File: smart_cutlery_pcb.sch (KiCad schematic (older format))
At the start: 0 parts

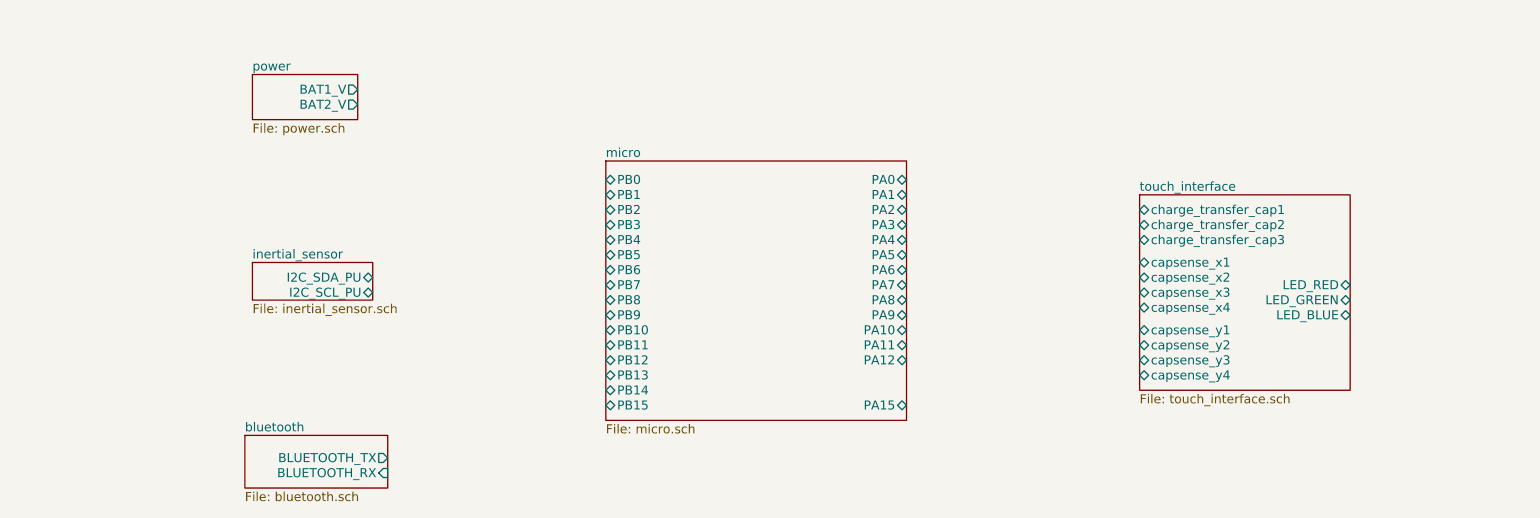
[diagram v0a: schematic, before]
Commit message: Make top-level connections between microcontroller and everything else
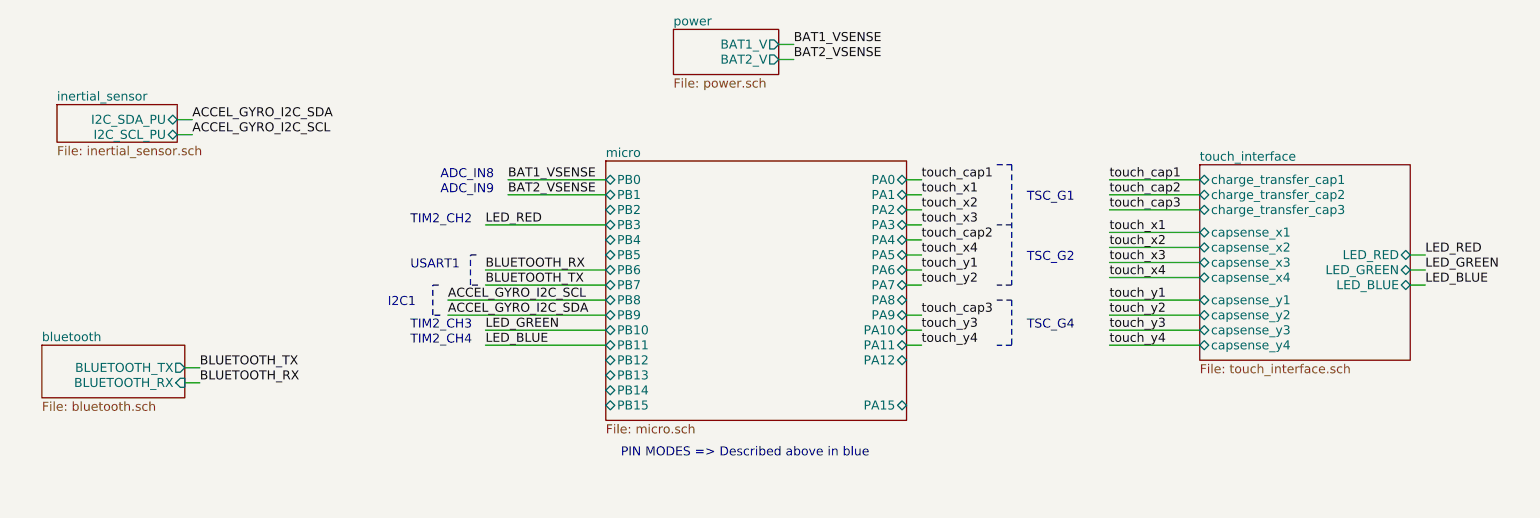
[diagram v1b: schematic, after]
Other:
- note added: "ADC_IN8"
- note added: "ADC_IN9"
- note added: "I2C1"
- note added: "PIN MODES => Described above in blue"
- note added: "TIM2_CH2"
- note added: "TIM2_CH3"
- note added: "TIM2_CH4\n"
- note added: "TSC_G1"
- note added: "TSC_G2"
- note added: "TSC_G4"
- note added: "USART1"

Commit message: Add optional bubble around intertial sensor pcb
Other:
- note added: "OPTIONAL"
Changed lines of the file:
@@
 Text Notes 5200 4850 0    60   ~ 0
 PIN MODES => Described above in blue
+Wire Notes Line
+	1150 2250 1150 3050
+Wire Notes Line
+	1150 3050 3500 3050
+Wire Notes Line
+	3500 3050 3500 2250
+Wire Notes Line
+	3500 2250 1150 2250
+Text Notes 2050 2200 0    60   ~ 0
+OPTIONAL
 $EndSCHEMATC

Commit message: Add switch footprints, add mode switch
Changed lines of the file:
@@
 F14 "LED_GREEN" B R 10450 3600 60
 F15 "LED_RED" B R 10450 3500 60
+F16 "mode_switch" B R 10450 3950 60
 $EndSheet
 Text Label 6350 2100 0    60   ~ 0
@@
 Text Notes 2050 2200 0    60   ~ 0
 OPTIONAL
+Text Label 10550 3950 0    60   ~ 0
+mode_switch
+Wire Wire Line
+	10550 3950 10450 3950
+Text Label 4300 4300 0    60   ~ 0
+mode_switch
+Wire Wire Line
+	4300 4300 5100 4300
 $EndSCHEMATC

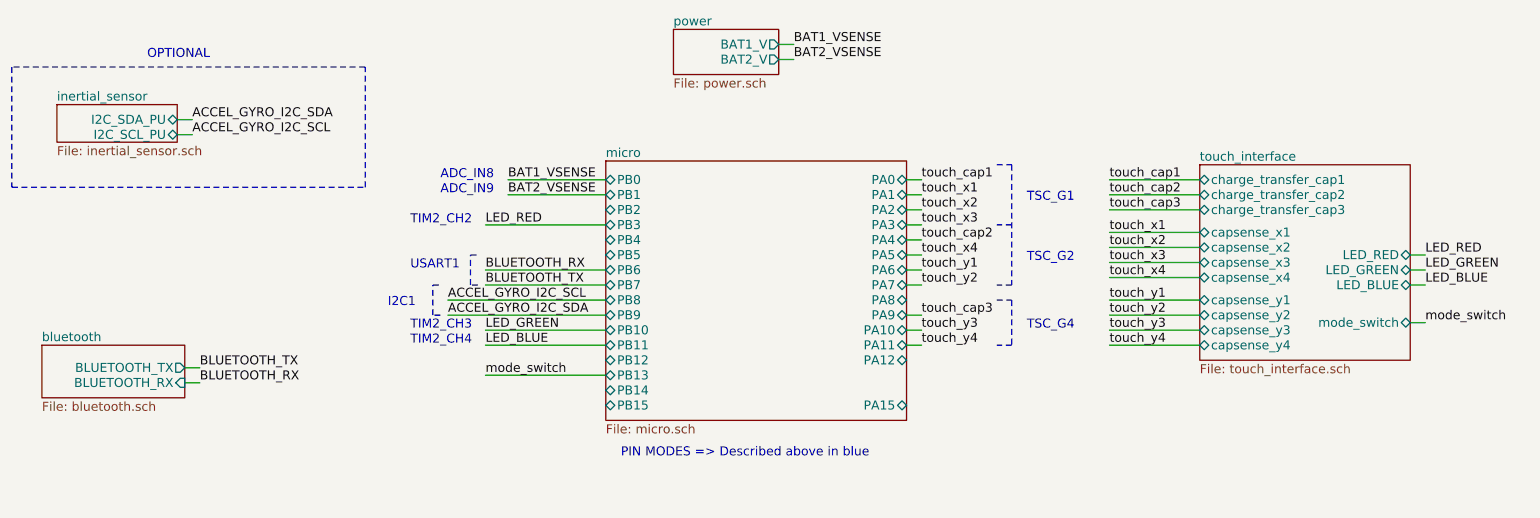
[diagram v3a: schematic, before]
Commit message: Update to new soft-latching power circuit
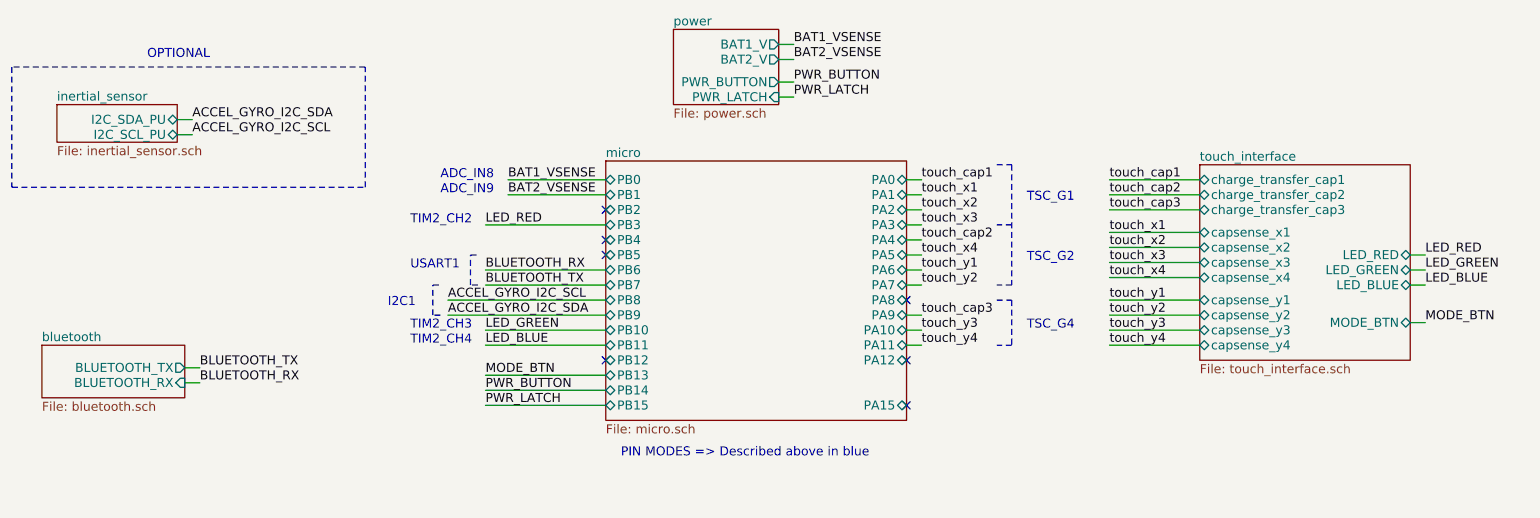
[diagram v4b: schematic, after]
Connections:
- no-connect marks 0 -> 7
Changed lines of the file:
@@
 $EndSheet
 $Sheet
-S 5550 2000 700  300
+S 5550 2000 700  500
 U 59A1225E
 F0 "power" 60
@@
 F2 "BAT1_V" O R 6250 2100 60
 F3 "BAT2_V" O R 6250 2200 60
+F4 "PWR_BUTTON" O R 6250 2350 60
+F5 "PWR_LATCH" I R 6250 2450 60
 $EndSheet
 $Sheet
@@
 F14 "LED_GREEN" B R 10450 3600 60
 F15 "LED_RED" B R 10450 3500 60
-F16 "mode_switch" B R 10450 3950 60
+F16 "MODE_BTN" B R 10450 3950 60
 $EndSheet
 Text Label 6350 2100 0    60   ~ 0
@@
 OPTIONAL
 Text Label 10550 3950 0    60   ~ 0
-mode_switch
+MODE_BTN
 Wire Wire Line
 	10550 3950 10450 3950
 Text Label 4300 4300 0    60   ~ 0
-mode_switch
+MODE_BTN
 Wire Wire Line
 	4300 4300 5100 4300
+Wire Wire Line
+	6250 2350 6350 2350
+Wire Wire Line
+	6250 2450 6350 2450
+Text Label 6350 2350 0    60   ~ 0
+PWR_BUTTON
+Text Label 6350 2450 0    60   ~ 0
+PWR_LATCH
+Text Label 4300 4400 0    60   ~ 0
+PWR_BUTTON
+Text Label 4300 4500 0    60   ~ 0
+PWR_LATCH
+Wire Wire Line
+	4300 4400 5100 4400
+Wire Wire Line
+	4300 4500 5100 4500
+NoConn ~ 5100 3400
+NoConn ~ 5100 3500
+NoConn ~ 5100 3200
+NoConn ~ 5100 4200
+NoConn ~ 7100 4200
+NoConn ~ 7100 4500
+NoConn ~ 7100 3800
 $EndSCHEMATC

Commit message: attempt 1
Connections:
- no-connect marks 7 -> 8
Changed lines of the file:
@@
 F14 "LED_GREEN" B R 10450 3600 60
 F15 "LED_RED" B R 10450 3500 60
-F16 "MODE_BTN" B R 10450 3950 60
 $EndSheet
 Text Label 6350 2100 0    60   ~ 0
@@
 Text Notes 2050 2200 0    60   ~ 0
 OPTIONAL
-Text Label 10550 3950 0    60   ~ 0
-MODE_BTN
-Wire Wire Line
-	10550 3950 10450 3950
-Text Label 4300 4300 0    60   ~ 0
-MODE_BTN
-Wire Wire Line
-	4300 4300 5100 4300
 Wire Wire Line
 	6250 2350 6350 2350
@@
 NoConn ~ 7100 4500
 NoConn ~ 7100 3800
+NoConn ~ 5100 4300
 $EndSCHEMATC

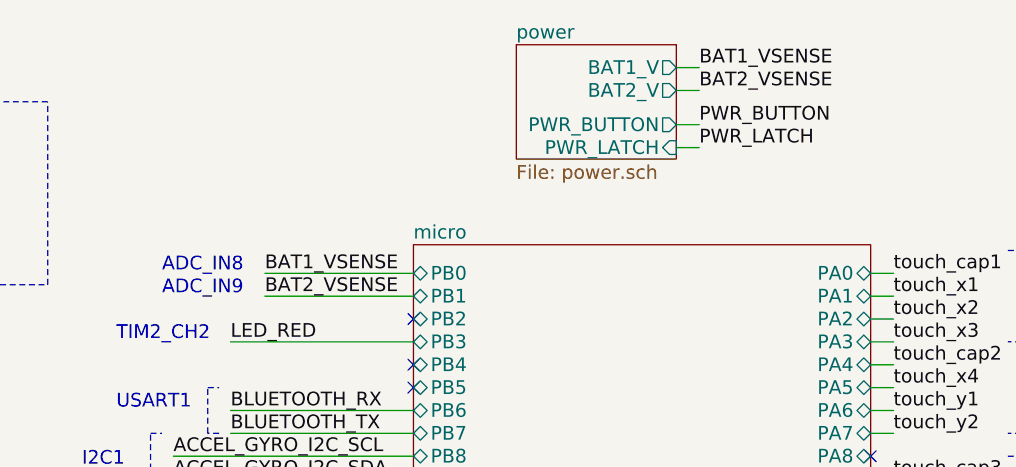
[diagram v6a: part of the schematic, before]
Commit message: Add boost converter test results
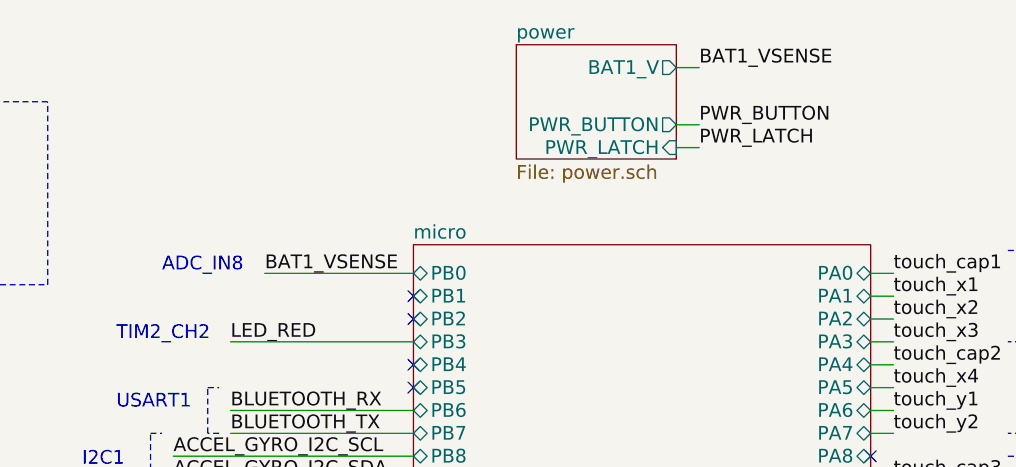
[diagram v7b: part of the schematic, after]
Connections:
- no-connect marks 8 -> 9
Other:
- note removed: "ADC_IN9"
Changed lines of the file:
@@
 $EndSheet
 $Sheet
-S 1350 4100 950 350
+S 1350 4100 950  350
 U 599FE73E
 F0 "bluetooth" 60
@@
 $EndSheet
 $Sheet
-S 5550 2000 700 500
+S 5550 2000 700  500
 U 59A1225E
 F0 "power" 60
 F1 "power.sch" 60
 F2 "BAT1_V" O R 6250 2100 60
-F3 "BAT2_V" O R 6250 2200 60
-F4 "PWR_BUTTON" O R 6250 2350 60
-F5 "PWR_LATCH" I R 6250 2450 60
-$EndSheet
-$Sheet
-S 1450 2500 800 250
+F3 "PWR_BUTTON" O R 6250 2350 60
+F4 "PWR_LATCH" I R 6250 2450 60
+$EndSheet
+$Sheet
+S 1450 2500 800  250
 U 59A2044A
 F0 "inertial_sensor" 60
@@
 Text Label 6350 2100 0    60   ~ 0
 BAT1_VSENSE
-Text Label 6350 2200 0    60   ~ 0
-BAT2_VSENSE
 Text Label 2350 2600 0    60   ~ 0
 ACCEL_GYRO_I2C_SDA
@@
 Text Label 4450 3000 0    60   ~ 0
 BAT1_VSENSE
-Text Label 4450 3100 0    60   ~ 0
-BAT2_VSENSE
 Text Label 4300 3300 0    60   ~ 0
 LED_RED
@@
 Text Notes 4000 3000 0    60   ~ 0
 ADC_IN8
-Text Notes 4000 3100 0    60   ~ 0
-ADC_IN9
 Text Notes 3800 3300 0    60   ~ 0
 TIM2_CH2
@@
 	6250 2100 6350 2100
 Wire Wire Line
-	6250 2200 6350 2200
-Wire Wire Line
 	2250 2600 2350 2600
 Wire Wire Line
@@
 Wire Wire Line
 	5100 3000 4450 3000
-Wire Wire Line
-	5100 3100 4450 3100
 Wire Wire Line
 	4300 3300 5100 3300
@@
 NoConn ~ 7100 3800
 NoConn ~ 5100 4300
+NoConn ~ 5100 3100
 $EndSCHEMATC
